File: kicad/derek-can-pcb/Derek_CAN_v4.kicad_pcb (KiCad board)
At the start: 2 copper layers, 50 x 25 mm, 8 parts, among them J1 FMHXG_RJ45NMCCFC, J2 PAN_SERVO, J3 LIFT_SERVO, J4 JST-XH-3, J5 JST-XH-3

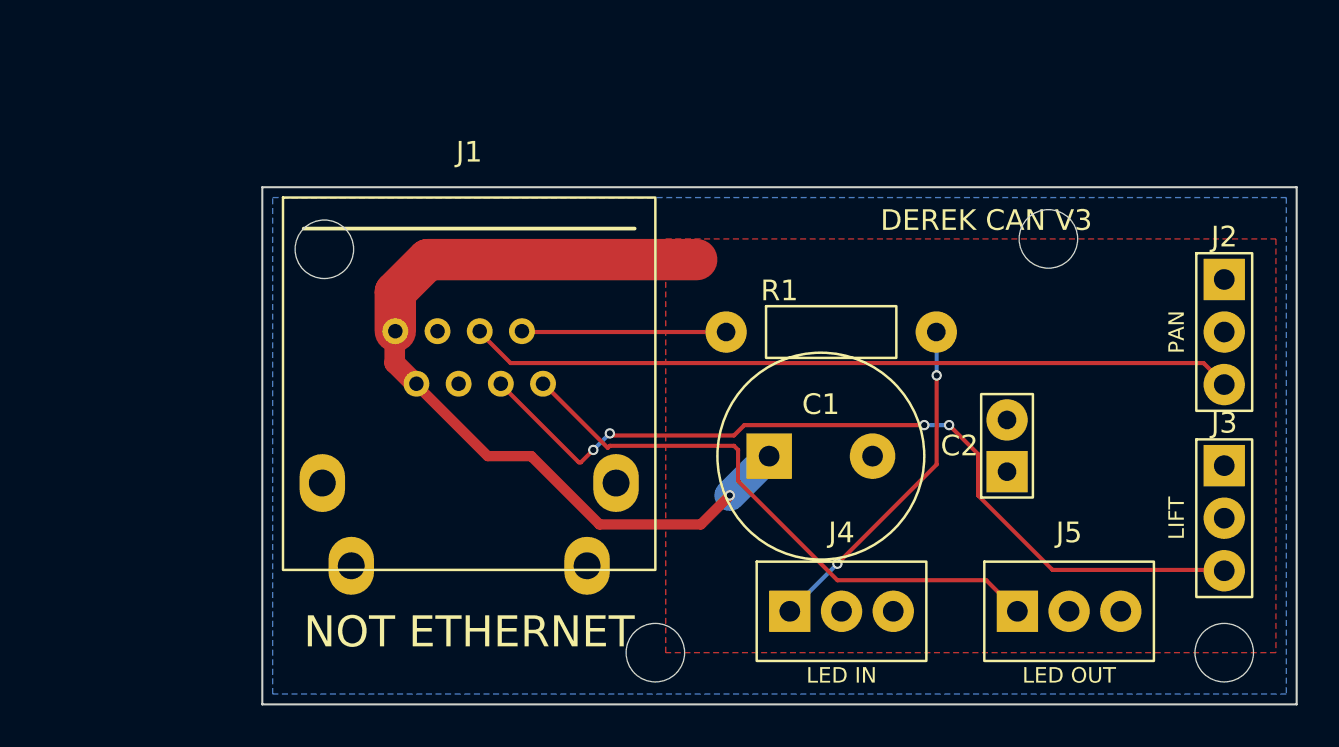
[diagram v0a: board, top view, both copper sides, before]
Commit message: REV 4 of CAN (4-layer) board - with correct RJ45 and better power distribution
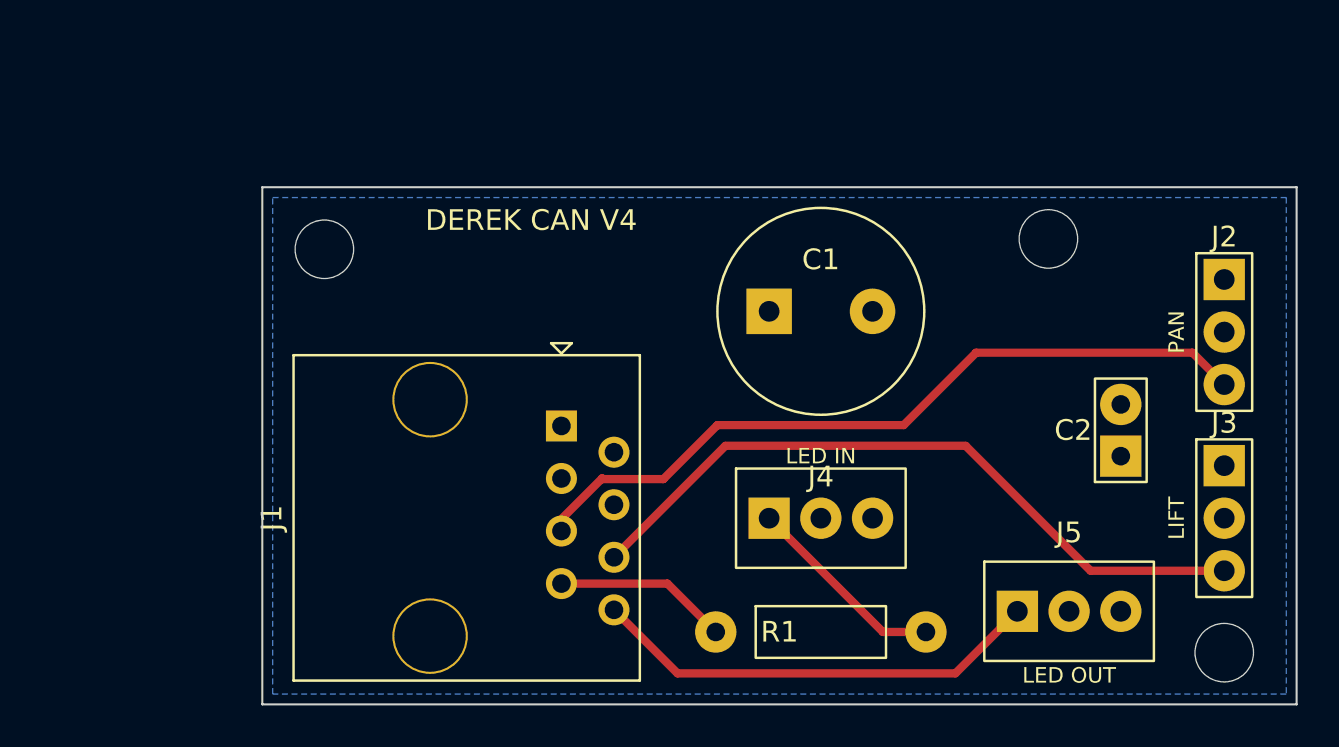
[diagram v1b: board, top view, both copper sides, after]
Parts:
- J1: footprint ClusterActual:FMHXG_RJ45NMCCFC_90D_RIGHT_ANGLE_8P8C_APPROX_VERIFY -> Connector_RJ:RJ45_OST_PJ012-8P8CX_Vertical
- moved R1 14.5 mm to (49.0, 40.5)
- moved C1 7.00 mm to (49.0, 25.0)
- moved C2 5.55 mm to (63.5, 30.8)
- moved J1 4.90 mm to (36.5, 30.5), turned to -90 degrees
- moved J4 4.61 mm to (49.0, 35.0)
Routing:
- net LIFT_PWM: track 41.5 -> 34.2 mm, vias 4 -> 0
- net LED_TO_FIRST: track 16.4 -> 9.86 mm, vias 2 -> 0
- net LED_RETURN_CLUSTER: track 28.4 -> 22.0 mm
- net 5V: track 41.5 -> 37.7 mm, vias 1 -> 0
- net LED_FROM_CLUSTER: track 9.80 -> 8.64 mm
- added copper zone on In2.Cu, net 5V
- added copper zone on In1.Cu, net GND
- removed copper zone on F.Cu, net 5V
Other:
- outline, holes or cut-outs redrawn
- copper layers 2 -> 4
- board text added: "DEREK CAN V4"
- board text removed: "DEREK CAN V3"

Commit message: Fixed RJ45 footprints on all, cleaned up routing, ready for a run at PCBWay
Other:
- board text added: "DEREK CAN V4a"
- board text removed: "DEREK CAN V4"
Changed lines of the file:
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@@
 		(capping no)
 		(filling no)
-		(zone_defaults)
 		(pcbplotparams
-			(layerselection 0x00000000_00000000_5555555f_f75555ff)
+			(layerselection 0x00000000_00000000_5555555f_ff5555ff)
 			(plot_on_all_layers_selection 0x00000000_00000000_00000000_00000000)
 			(disableapertmacros no)
@@
 		)
 		(property "Value" "100nF 50V X7R"
-			(at 3 2 0)
+			(at 3 -0.5 0)
 			(layer "F.Fab")
 			(effects
@@
 		)
 		(property "Value" "LIFT_SERVO"
-			(at -5 -2 0)
+			(at 2 0 90)
 			(layer "F.Fab")
 			(effects
@@
 		(at 49 35)
 		(property "Reference" "J4"
-			(at 0 -2 0)
+			(at 4 -3 0)
 			(layer "F.SilkS")
 			(effects
@@
 		)
 		(property "Value" "PAN_SERVO"
-			(at -5 -2.5 0)
+			(at 2 0 90)
 			(layer "F.Fab")
 			(effects
@@
 		(layer "Edge.Cuts")
 	)
-	(gr_text "DEREK CAN V4"
+	(gr_text "RJ45 NOT ETHERNET - 5V POWER"
+		(at 33 25.5 -0)
+		(layer "F.SilkS")
+		(effects
+			(font
+				(size 0.8 0.8)
+				(thickness 0.12)
+			)
+		)
+	)
+	(gr_text "DEREK CAN V4a"
 		(at 35 20.6 0)
 		(layer "F.SilkS")
@@
 	)
 	(gr_text "RJ45 NOT ETHERNET - 5V POWER"
-		(at 55.5 43 0)
+		(at 33 25.5 0)
 		(layer "B.SilkS")
 		(effects

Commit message: Fixed servo controller footprint, submitted to JLCPCB today
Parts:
- moved C1 12.2 mm to (39.0, 18.0)
- moved C2 12.2 mm to (53.5, 23.8)
- moved J1 12.2 mm to (26.5, 23.5)
- moved J2 12.2 mm to (58.5, 19.0)
- moved J3 12.2 mm to (58.5, 28.0)
- moved J4 12.2 mm to (39.0, 28.0)
- moved J5 12.2 mm to (51.0, 32.5)
- moved R1 12.2 mm to (39.0, 33.5)
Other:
- board text added: "DEREK CAN V4b"
- board text removed: "DEREK CAN V4a"
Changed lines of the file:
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@@
 	(footprint "Capacitor_THT:C_Disc_D5.0mm_W2.5mm_P2.50mm"
 		(layer "F.Cu")
-		(at 63.5 30.75 90)
+		(at 53.5 23.75 90)
 		(property "Reference" "C2"
 			(at 0 -2.3 0)
@@
 	(footprint "Connector_PinHeader_2.54mm:PinHeader_1x03_P2.54mm_Vertical"
 		(layer "F.Cu")
-		(at 68.5 35)
+		(at 58.5 28)
 		(property "Reference" "J3"
 			(at 0 -4.6 0)
@@
 	(footprint "Connector_RJ:RJ45_OST_PJ012-8P8CX_Vertical"
 		(layer "F.Cu")
-		(at 36.46 30.54 -90)
+		(at 26.46 23.54 -90)
 		(descr "RJ45 vertical connector https://www.on-shore.com/wp-content/uploads/PJ012-8P8CX.pdf")
 		(tags "RJ45 PJ012")
@@
 	(footprint "Capacitor_THT:CP_Radial_D10.0mm_P5.00mm"
 		(layer "F.Cu")
-		(at 49 25)
+		(at 39 18)
 		(property "Reference" "C1"
 			(at 0 -2.5 0)
@@
 	(footprint "Connector_JST:JST_XH_B3B-XH-A_1x03_P2.50mm_Vertical"
 		(layer "F.Cu")
-		(at 61 39.5)
+		(at 51 32.5)
 		(property "Reference" "J5"
 			(at 0 -3.8 0)
@@
 	(footprint "Connector_JST:JST_XH_B3B-XH-A_1x03_P2.50mm_Vertical"
 		(layer "F.Cu")
-		(at 49 35)
+		(at 39 28)
 		(property "Reference" "J4"
 			(at 4 -3 0)
@@
 	(footprint "Connector_PinHeader_2.54mm:PinHeader_1x03_P2.54mm_Vertical"
 		(layer "F.Cu")
-		(at 68.5 26)
+		(at 58.5 19)
 		(property "Reference" "J2"
 			(at 0 -4.6 0)
@@
 	(footprint "Resistor_THT:R_Axial_DIN0207_L6.3mm_D2.5mm_P10.16mm_Horizontal"
 		(layer "F.Cu")
-		(at 49 40.5)
+		(at 39 33.5)
 		(property "Reference" "R1"
 			(at -2 0 0)
@@
 	)
 	(gr_rect
-		(start 22 19)
-		(end 72 44)
+		(start 12 12)
+		(end 62 37)
 		(stroke
 			(width 0.1)
@@
 	)
 	(gr_circle
-		(center 25 22)
-		(end 26 23)
+		(center 15 15)
+		(end 16 16)
 		(stroke
 			(width 0.05)
@@
 	)
 	(gr_circle
-		(center 60 21.5)
-		(end 61 22.5)
+		(center 50 14.5)
+		(end 51 15.5)
 		(stroke
 			(width 0.05)
@@
 	)
 	(gr_circle
-		(center 68.5 41.5)
-		(end 69.5 42.5)
+		(center 58.5 34.5)
+		(end 59.5 35.5)
 		(stroke
 			(width 0.05)
@@
 	)
 	(gr_text "RJ45 NOT ETHERNET - 5V POWER"
-		(at 33 25.5 -0)
+		(at 23 18.5 -0)
 		(layer "F.SilkS")
 		(effects
@@
 		)
 	)
-	(gr_text "DEREK CAN V4a"
-		(at 35 20.6 0)
+	(gr_text "DEREK CAN V4b"
+		(at 25 13.6 0)
 		(layer "F.SilkS")
 		(effects
@@
 	)
 	(gr_text "RJ45 NOT ETHERNET - 5V POWER"
-		(at 33 25.5 0)
+		(at 23 18.5 0)
 		(layer "B.SilkS")
 		(effects
@@
 	)
 	(segment
-		(start 68.5 35)
-		(end 64.5 35)
+		(start 58.5 28)
+		(end 54.5 28)
 		(width 2)
 		(layer "In2.Cu")
@@
 	)
 	(segment
-		(start 68.5 26)
-		(end 64.5 26)
+		(start 58.5 19)
+		(end 54.5 19)
 		(width 2)
 		(layer "In2.Cu")
@@
 	)
 	(segment
-		(start 40.69 31.81)
-		(end 46.5 26)
+		(start 30.69 24.81)
+		(end 36.5 19)
 		(width 1.5)
 		(layer "In2.Cu")
@@
 	)
 	(segment
-		(start 49 35)
-		(end 49 32)
+		(start 39 28)
+		(end 39 25)
 		(width 2)
 		(layer "In2.Cu")
@@
 	)
 	(segment
-		(start 39 31.81)
-		(end 40.69 31.81)
+		(start 29 24.81)
+		(end 30.69 24.81)
 		(width 1.5)
 		(layer "In2.Cu")
@@
 	)
 	(segment
-		(start 61 39.5)
-		(end 61 36)
+		(start 51 32.5)
+		(end 51 29)
 		(width 2)
 		(layer "In2.Cu")
@@
 	)
 	(segment
-		(start 46.5 26)
-		(end 46.5 25)
+		(start 36.5 19)
+		(end 36.5 18)
 		(width 1.5)
 		(layer "In2.Cu")
@@
 	)
 	(segment
-		(start 42 25)
-		(end 46.5 25)
+		(start 32 18)
+		(end 36.5 18)
 		(width 1.5)
 		(layer "In2.Cu")
@@
 	)
 	(segment
-		(start 36.46 30.54)
-		(end 42 25)
+		(start 26.46 23.54)
+		(end 32 18)
 		(width 1.5)
 		(layer "In2.Cu")
@@
 	)
 	(segment
-		(start 62.04 37.54)
-		(end 68.5 37.54)
+		(start 52.04 30.54)
+		(end 58.5 30.54)
 		(width 0.4)
 		(layer "F.Cu")
@@
 	)
 	(segment
-		(start 56 31.5)
-		(end 62.04 37.54)
+		(start 46 24.5)
+		(end 52.04 30.54)
 		(width 0.4)
 		(layer "F.Cu")
@@
 	)
 	(segment
-		(start 39 36.89)
-		(end 44.39 31.5)
+		(start 29 29.89)
+		(end 34.39 24.5)
 		(width 0.4)
 		(layer "F.Cu")
@@
 	)
 	(segment
-		(start 44.39 31.5)
-		(end 56 31.5)
+		(start 34.39 24.5)
+		(end 46 24.5)
 		(width 0.4)
 		(layer "F.Cu")
@@
 	)
 	(segment
-		(start 53 30.5)
-		(end 56.5 27)
+		(start 43 23.5)
+		(end 46.5 20)
 		(width 0.4)
 		(layer "F.Cu")
@@
 	)
 	(segment
-		(start 36.46 35.62)
-		(end 36.46 35.04)
+		(start 26.46 28.62)
+		(end 26.46 28.04)
 		(width 0.4)
 		(layer "F.Cu")
@@
 	)
 	(segment
-		(start 41.39 33.11)
-		(end 44 30.5)
+		(start 31.39 26.11)
+		(end 34 23.5)
 		(width 0.4)
 		(layer "F.Cu")
@@
 	)
 	(segment
-		(start 44 30.5)
-		(end 53 30.5)
+		(start 34 23.5)
+		(end 43 23.5)
 		(width 0.4)
 		(layer "F.Cu")
@@
 	)
 	(segment
-		(start 36.46 35.04)
-		(end 38.425761 33.074239)
+		(start 26.46 28.04)
+		(end 28.425761 26.074239)
 		(width 0.4)
 		(layer "F.Cu")
@@
 	)
 	(segment
-		(start 38.425761 33.074239)
-		(end 38.461522 33.11)
+		(start 28.425761 26.074239)
+		(end 28.461522 26.11)
 		(width 0.4)
 		(layer "F.Cu")
@@
 	)
 	(segment
-		(start 38.461522 33.11)
-		(end 41.39 33.11)
+		(start 28.461522 26.11)
+		(end 31.39 26.11)
 		(width 0.4)
 		(layer "F.Cu")
@@
 	)
 	(segment
-		(start 56.5 27)
-		(end 66.96 27)
+		(start 46.5 20)
+		(end 56.96 20)
 		(width 0.4)
 		(layer "F.Cu")
@@
 	)
 	(segment
-		(start 66.96 27)
-		(end 68.5 28.54)
+		(start 56.96 20)
+		(end 58.5 21.54)
 		(width 0.4)
 		(layer "F.Cu")
@@
 	)
 	(segment
-		(start 41.58 38.16)
-		(end 43.92 40.5)
+		(start 31.58 31.16)
+		(end 33.92 33.5)
 		(width 0.4)
 		(layer "F.Cu")
@@
 	)
 	(segment
-		(start 36.46 38.16)
-		(end 41.58 38.16)
+		(start 26.46 31.16)
+		(end 31.58 31.16)
 		(width 0.4)
 		(layer "F.Cu")
@@
 	)
 	(segment
-		(start 36.46 38.16)
-		(end 36.46 37.945075)
+		(start 26.46 31.16)
+		(end 26.46 30.945075)
 		(width 0.4)
 		(layer "F.Cu")
@@
 	)
 	(segment
-		(start 39 39.43)
-		(end 42.07 42.5)
+		(start 29 32.43)
+		(end 32.07 35.5)
 		(width 0.4)
 		(layer "F.Cu")
@@
 	)
 	(segment
-		(start 55.5 42.5)
-		(end 58.5 39.5)
+		(start 45.5 35.5)
+		(end 48.5 32.5)
 		(width 0.4)
 		(layer "F.Cu")
@@
 	)
 	(segment
-		(start 42.07 42.5)
-		(end 55.5 42.5)
+		(start 32.07 35.5)
+		(end 45.5 35.5)
 		(width 0.4)
 		(layer "F.Cu")
@@
 	)
 	(segment
-		(start 54.08 40.5)
-		(end 52 40.5)
+		(start 44.08 33.5)
+		(end 42 33.5)
 		(width 0.4)
 		(layer "F.Cu")
@@
 	)
 	(segment
-		(start 52 40.5)
-		(end 46.5 35)
+		(start 42 33.5)
+		(end 36.5 28)
 		(width 0.4)
 		(layer "F.Cu")
@@
 		(polygon
 			(pts
-				(xy 22.5 19.5) (xy 71.5 19.5) (xy 71.5 43.5) (xy 22.5 43.5)
+				(xy 12.5 12.5) (xy 61.5 12.5) (xy 61.5 36.5) (xy 12.5 36.5)
 			)
 		)
@@
 		(polygon
 			(pts
-				(xy 22.5 19.5) (xy 71.5 19.5) (xy 71.5 43.5) (xy 22.5 43.5)
+				(xy 12.5 12.5) (xy 61.5 12.5) (xy 61.5 36.5) (xy 12.5 36.5)
 			)
 		)
@@
 		(polygon
 			(pts
-				(xy 34 31.5) (xy 37.5 31.5) (xy 38 32.5) (xy 38.5 32.5) (xy 40 33) (xy 46.5 27.5) (xy 48 27.5) (xy 48 36)
-				(xy 50.5 36) (xy 50.5 31.5) (xy 56 31.5) (xy 58 34.5) (xy 60 37) (xy 60 39.5) (xy 62 39.5) (xy 62 37.066667)
-				(xy 70 36) (xy 70 34) (xy 65.5 33) (xy 65.5 27.5) (xy 69 27.15) (xy 69.475246 25.304951) (xy 55 22.5)
-				(xy 40.673419 22.562463) (xy 34.032707 29.800723)
-			)
-		)
+				(xy 24 24.5) (xy 27.5 24.5) (xy 28 25.5) (xy 28.5 25.5) (xy 30 26) (xy 36.5 20.5) (xy 38 20.5) (xy 38 29)
+				(xy 40.5 29) (xy 40.5 24.5) (xy 46 24.5) (xy 48 27.5) (xy 50 30) (xy 50 32.5) (xy 52 32.5) (xy 52 30.066667)
+				(xy 60 29) (xy 60 27) (xy 55.5 26) (xy 55.5 20.5) (xy 59 20.15) (xy 59.475246 18.304951) (xy 45 15.5)
+				(xy 30.673419 15.562463) (xy 24.032707 22.800723)
+			)
+		)
